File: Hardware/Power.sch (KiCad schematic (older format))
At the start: 0 parts

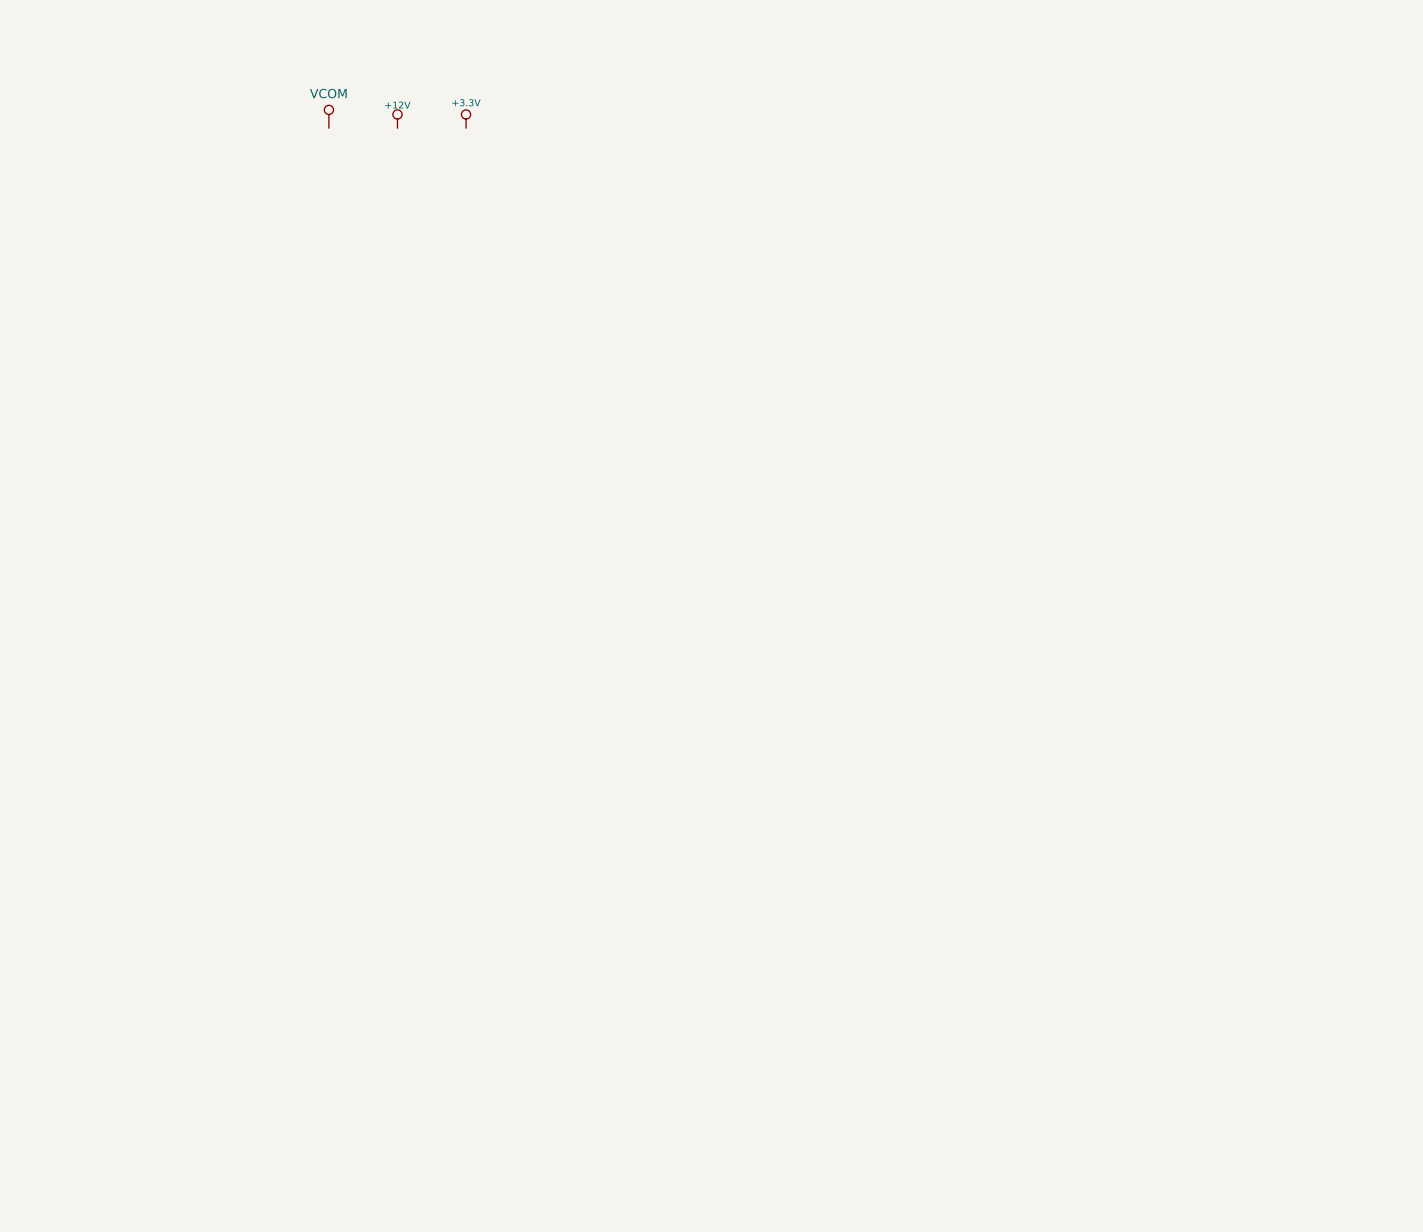
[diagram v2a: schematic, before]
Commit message: Add 12v regulator and populate BOM fields
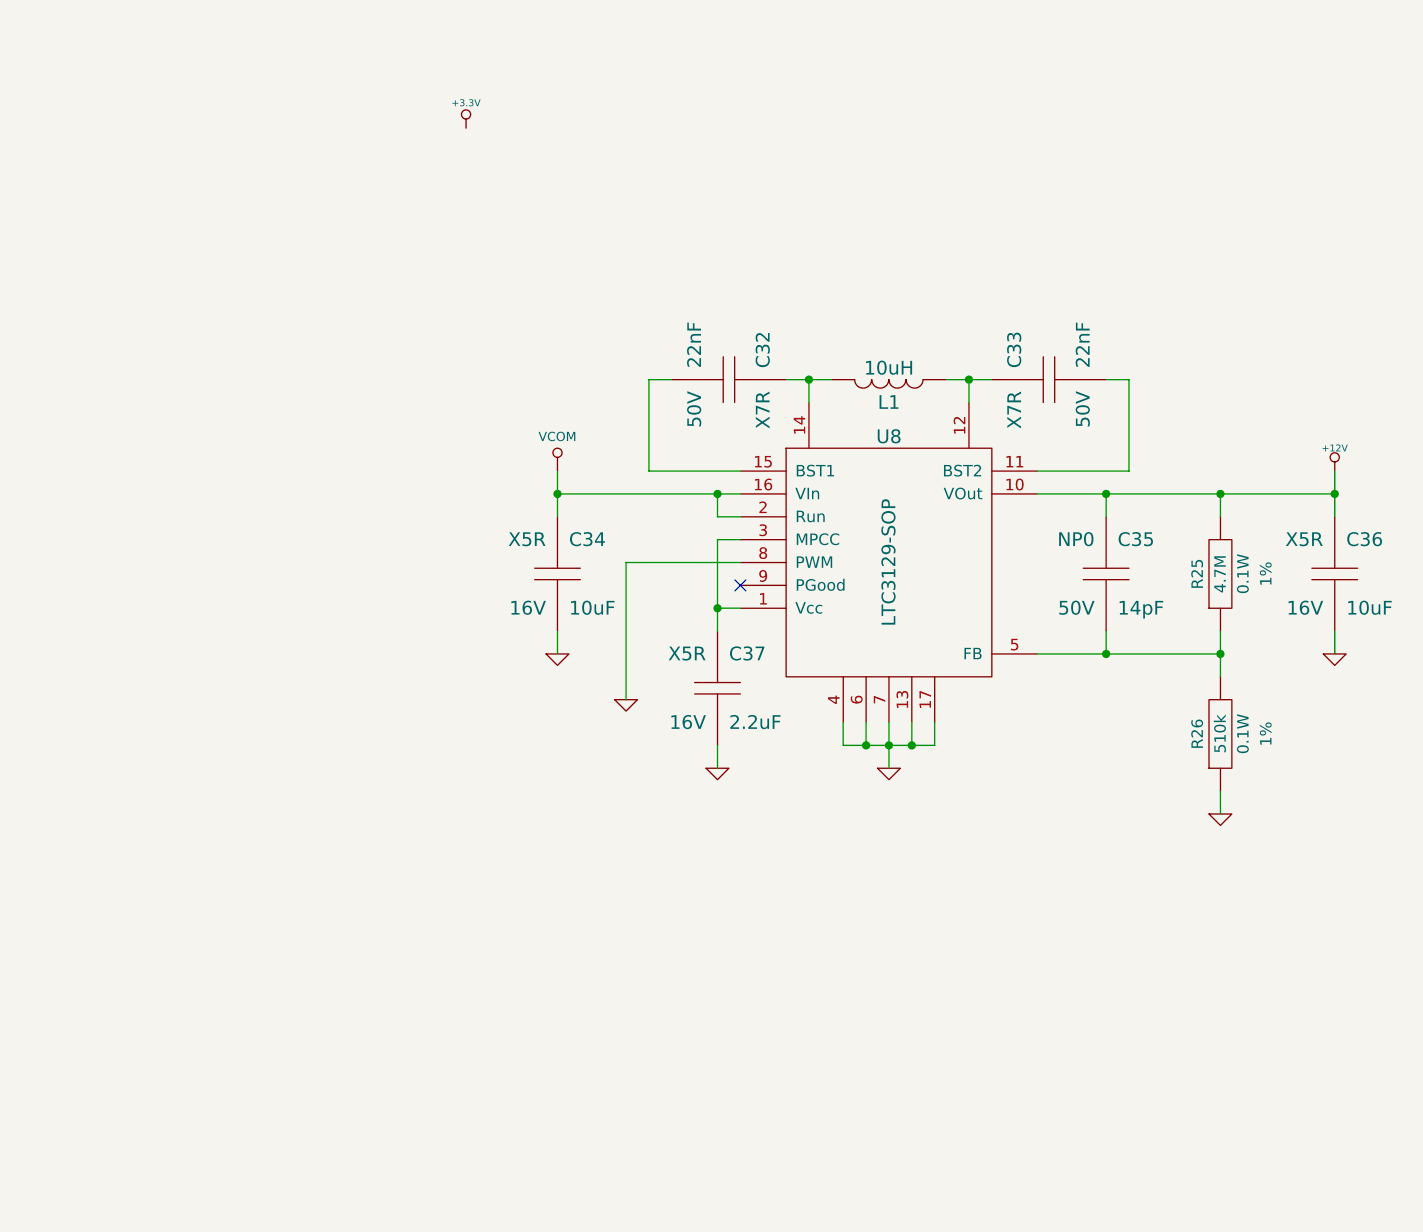
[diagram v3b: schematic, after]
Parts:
- added C32, C33: 22nF, ~, symbol C
- added C34, C36: 10uF, ~, symbol C
- added C35: 14pF, ~, symbol C
- added C37: 2.2uF, ~, symbol C
- added L1: 10uH, INDC3225, symbol L
- added R25: 4.7M, ~, symbol R
- added R26: 510k, ~, symbol R
- added U8: LTC3129-SOP, symbol LTC3129-SOP
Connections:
- net +12V: now also C35.1, C36.1, R25.2, U8.10 (VOut)
- net VCOM: now also C34.1, U8.16 (VIn), U8.2 (Run)
- new net: C32.1, L1.1, U8.14
- new net: C33.1, L1.2, U8.12
- new net: C32.2, U8.15 (BST1)
- new net: C35.2, R25.1, R26.2, U8.5 (FB)
- new net: C37.1, U8.1 (Vcc), U8.3 (MPCC)
- new net: C33.2, U8.11 (BST2)
- new net GND: C34.2, C36.2, C37.2, R26.1, U8.13, U8.17, U8.4, U8.6, U8.7, U8.8 (PWM)
- no-connect marks 0 -> 1

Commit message: Add 3.3v regulator and populate BOM fields
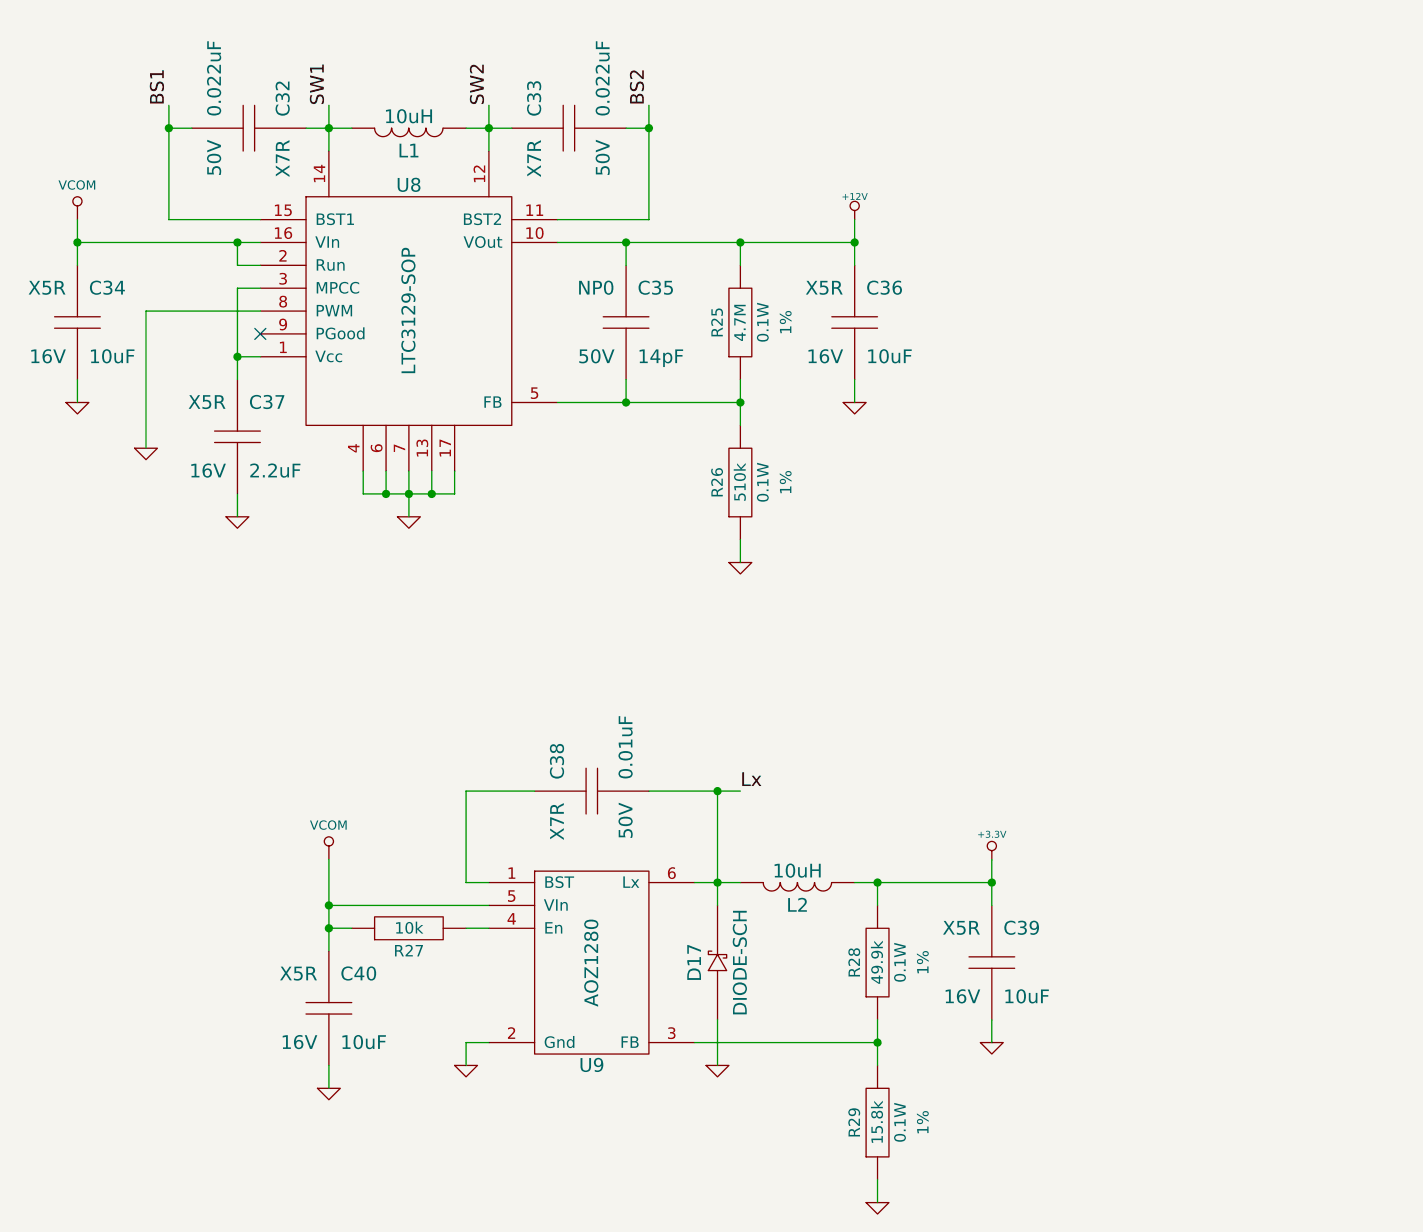
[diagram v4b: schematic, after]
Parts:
- added C38: 0.01uF, CAPC1608, symbol C
- added C39, C40: 10uF, ~, symbol C
- added D17: DIODE-SCH, ~, symbol DIODE-SCH
- added L2: 10uH, INDC3225, symbol L
- added R27: 10k, ~, symbol R
- added R28: 49.9k, RESC1608, symbol R
- added R29: 15.8k, RESC1608, symbol R
- added U9: AOZ1280, symbol AOZ1280
- C32, C33: value 22nF -> 0.022uF
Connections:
- net +3.3V: now also C39.1, L2.2, R28.2
- net GND: now also C39.2, C40.2, D17.1, R29.1, U9.2 (Gnd)
- net VCOM: now also C40.1, R27.1, U9.5 (VIn)
- net SW1: now reaches C32.1, L1.1, U8.14
- net SW2: now reaches C33.1, L1.2, U8.12
- net BS1: now reaches C32.2, U8.15 (BST1)
- net BS2: now reaches C33.2, U8.11 (BST2)
- new net: C38.1, U9.1 (BST)
- new net: R28.1, R29.2, U9.3 (FB)
- new net: R27.2, U9.4 (En)
- new net Lx: C38.2, D17.2, L2.1, U9.6 (Lx)
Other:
- moved on the sheet: C32, C33, C34, C35, C36, C37, L1, R25, R26, U8

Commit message: Reannotate
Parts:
- added R30: 10k, ~, symbol R
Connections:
- net VCOM: now also R30.1; no longer U8.2 (Run)
- new net: R30.2, U8.2 (Run)
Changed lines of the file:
@@
 Sheet 8 8
 Title ""
-Date "27 sep 2013"
+Date "8 dec 2013"
 Rev ""
 Comp ""
@@
 $EndComp
 Wire Wire Line
-	1300 2100 2100 2100
-Wire Wire Line
 	1300 2000 1300 2200
-Wire Wire Line
-	2100 2200 2000 2200
-Wire Wire Line
-	2000 2200 2000 2100
-Connection ~ 2000 2100
 Wire Wire Line
 	1800 1600 1700 1600
@@
 	1    0    0    -1
 $EndComp
+Wire Wire Line
+	2100 2100 1300 2100
+$Comp
+L R R30
+U 1 1 52A3E59A
+P 1750 2200
+F 0 "R30" H 1750 2300 50  0000 C CNN
+F 1 "10k" H 1750 2200 50  0000 C CNN
+F 2 "~" H 1750 2200 60  0000 C CNN
+F 3 "~" H 1750 2200 60  0000 C CNN
+F 4 "W" H 1750 2100 50  0001 C CNN "Power"
+F 5 "%" H 1750 2000 50  0001 C CNN "Tolerance"
+	1    1750 2200
+	1    0    0    1
+$EndComp
+Wire Wire Line
+	1500 2200 1400 2200
+Wire Wire Line
+	1400 2200 1400 2100
+Connection ~ 1400 2100
+Wire Wire Line
+	2000 2200 2100 2200
 $EndSCHEMATC

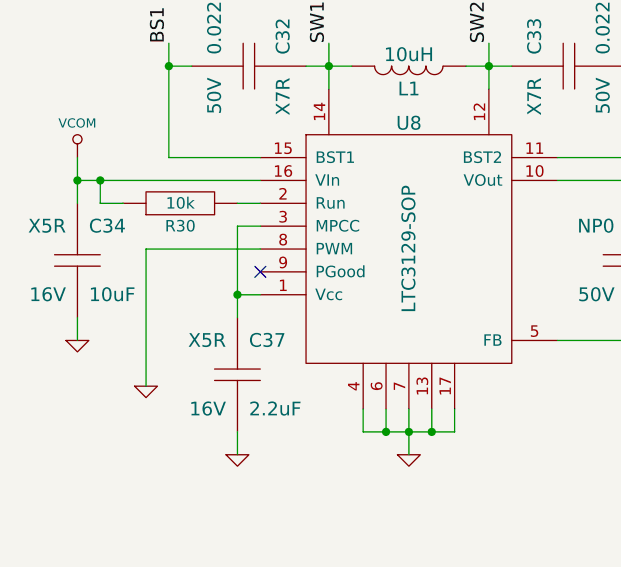
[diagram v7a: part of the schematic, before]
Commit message: Change to vertical USB port
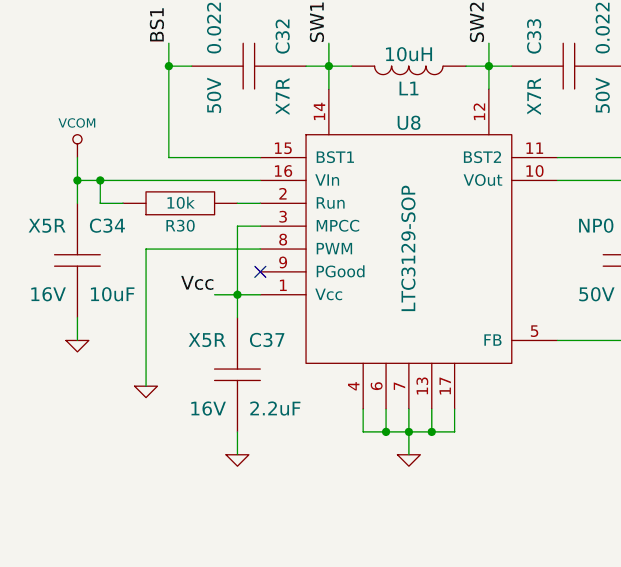
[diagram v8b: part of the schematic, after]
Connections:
- net Vcc: now reaches C37.1, U8.1 (Vcc), U8.3 (MPCC)
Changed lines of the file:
@@
 Sheet 8 8
 Title ""
-Date "21 dec 2013"
+Date "22 dec 2013"
 Rev ""
 Comp ""
@@
 Connection ~ 4200 2800
 Wire Wire Line
-	2100 2600 2000 2600
+	1900 2600 2100 2600
 Wire Wire Line
 	2000 2300 2000 2700
@@
 Wire Wire Line
 	2000 2200 2100 2200
+Text Label 1900 2600 2    60   ~ 0
+Vcc
 $EndSCHEMATC
